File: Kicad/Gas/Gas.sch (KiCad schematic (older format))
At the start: 9 parts, among them J1 MG811, J2 Arduino, J3 MQ135

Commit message: Added air quality sensor to Kicad Gas schematic. Added code for CCS811. Note: arduino program is temporarily not compiling.
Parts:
- added J4: CCS811, Socket_Strips:Socket_Strip_Angled_1x07_Pitch2.54mm, symbol CONN_01X07
- J2: symbol Screw_Terminal_1x06 -> Screw_Terminal_1x10
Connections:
- net +3V3: now also J4.2 (P2)
- net +5V: now also J2.9; no longer J2.3
- net GND: now also J4.1 (P1)
- net Vout: now also J2.3; no longer J2.4
- net at J1.3 (P3): now also J2.10; no longer J2.5
- net nWAKE: now reaches J2.6
- net nWAKE: now also J4.5 (P5)
- new net SCL: J2.5, J4.4 (P4)
- new net SDA: J2.4, J4.3 (P3)
- new net nINT: J2.7, J4.6 (P6)
- new net nRST: J2.8, J4.7 (P7)
- no-connect marks 3 -> 2
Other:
- moved on the sheet: C1, C2, D1, J1, J3, R1, R2, R3

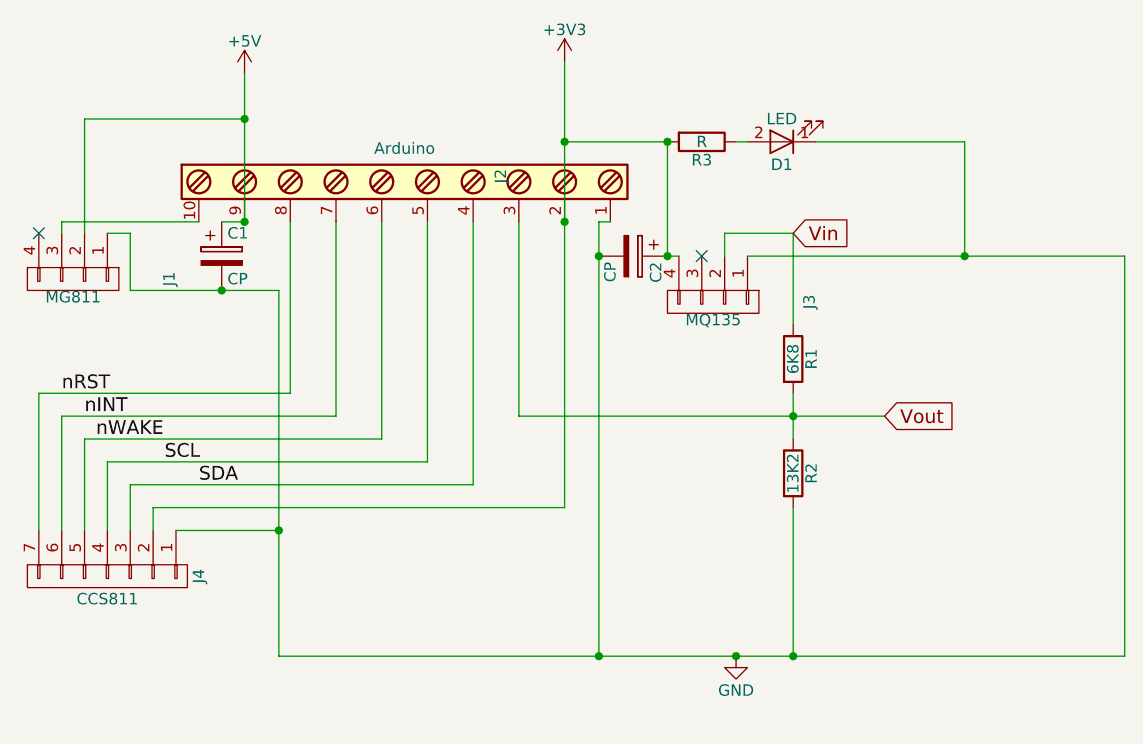
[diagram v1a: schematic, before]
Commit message: Temperature and Temperature+RH (TTRH) sensors are all implemented. All sensors were tested, except Thermopar temperature sensor. Added TTRH shield schematic and layout (missing SDA1 and SCL1 for SHT75).
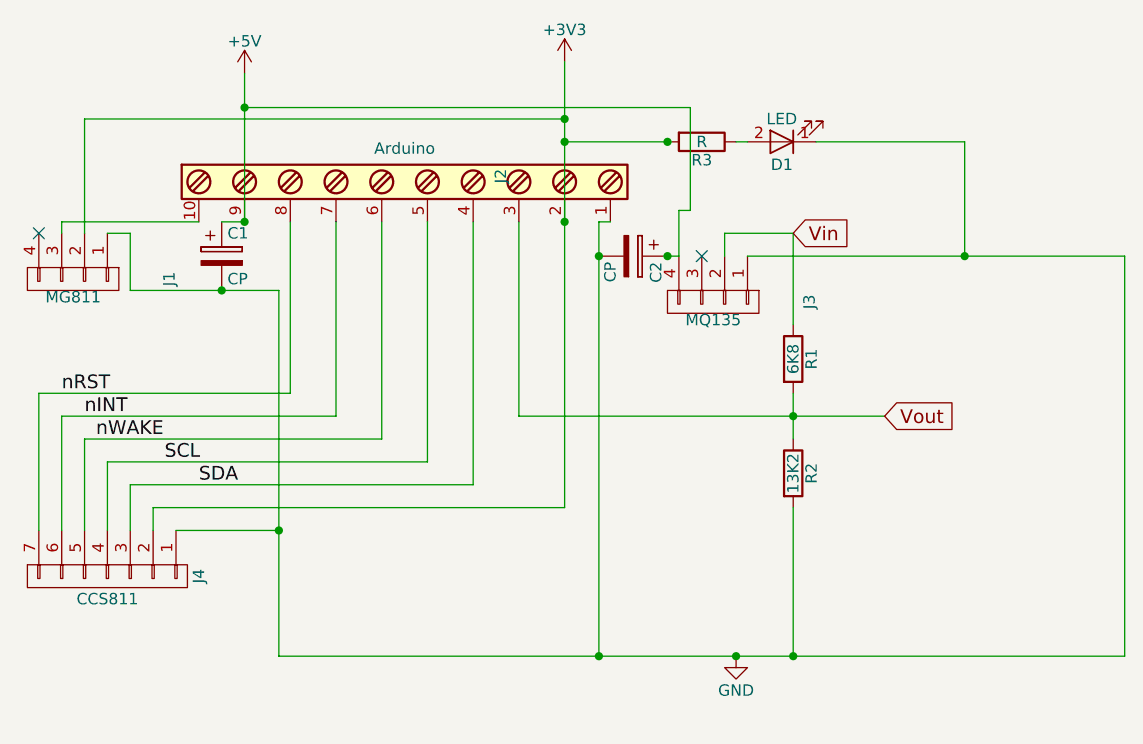
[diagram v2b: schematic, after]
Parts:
- J2: footprint Connectors_Terminal_Blocks:TerminalBlock_Pheonix_MPT-2.54mm_6pol -> Connectors_Terminal_Blocks:TerminalBlock_Pheonix_MPT-2.54mm_10pol
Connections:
- net +3V3: now also J1.2 (P2); no longer C2.1, J3.4 (P4)
- net +5V: now also C2.1, J3.4 (P4); no longer J1.2 (P2)
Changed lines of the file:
@@
 F 0 "J2" H 3050 1700 50  0000 C TNN
 F 1 "Arduino" V 2900 1250 50  0000 C TNN
-F 2 "Connectors_Terminal_Blocks:TerminalBlock_Pheonix_MPT-2.54mm_6pol" H 3050 825 50  0001 C CNN
+F 2 "Connectors_Terminal_Blocks:TerminalBlock_Pheonix_MPT-2.54mm_10pol" H 3050 825 50  0001 C CNN
 F 3 "" H 3025 1450 50  0001 C CNN
 	1    3050 1250
@@
 	4250 1600 4200 1600
 Wire Wire Line
-	4200 1600 4200 1100
-Wire Wire Line
 	4200 1100 3750 1100
 Connection ~ 3750 1100
-Wire Wire Line
-	1650 1000 2350 1000
 Wire Wire Line
 	2350 800  2350 1450
@@
 Wire Wire Line
 	2350 1450 2250 1450
-Connection ~ 2350 1000
 Connection ~ 2350 1450
 Wire Wire Line
@@
 	1450 2200 1450 2800
 Connection ~ 4750 3350
+Wire Wire Line
+	1650 1000 3750 1000
+Connection ~ 3750 1000
+Wire Wire Line
+	4250 1600 4250 1400
+Wire Wire Line
+	4250 1400 4300 1400
+Wire Wire Line
+	4300 1400 4300 950
+Wire Wire Line
+	4300 950  2350 950
+Connection ~ 2350 950
 $EndSCHEMATC

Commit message: Corrected kicad libraries. Added ecoPlanos libs.
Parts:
- removed J2: Arduino, Connectors_Terminal_Blocks:TerminalBlock_Pheonix_MPT-2.54mm_10pol, symbol Screw_Terminal_1x10
- added J2, J5: CONN_01X04, symbol CONN_01X04
- added J6, J7: CONN_01X02, symbol CONN_01X02
- D1: symbol LED -> LED-RESCUE-Gas
- J1: footprint Socket_Strips:Socket_Strip_Angled_1x04_Pitch2.54mm -> Pin_Headers:Pin_Header_Straight_1x03_Pitch1.00mm
- J3: footprint Socket_Strips:Socket_Strip_Angled_1x04_Pitch2.54mm -> Pin_Headers:Pin_Header_Straight_1x04_Pitch2.54mm
- R1, R2, R3: symbol R -> R-RESCUE-Gas
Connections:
- net +3V3: now also C1.1, J6.1 (P1)
- net +5V: now also J7.1 (P1); no longer C1.1
- net GND: now also J6.2 (P2), J7.2 (P2)
- net SCL: now also J5.1 (P1)
- net SDA: now also J5.2 (P2)
- net Vout: now also J5.3 (P3)
- net nINT: now also J2.3 (P3)
- net nRST: now also J2.2 (P2)
- net nWAKE: now also J2.4 (P4)
- net at J1.3 (P3): now also J5.4 (P4)
- net Vin: no longer names the net of J3.2 (P2), R1.1
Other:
- moved on the sheet: C1, C2, D1, J1, R3

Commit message: Added PH4 connectors libs; Finshed CO2 sensors schematic circuit.
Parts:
- J2: value CONN_01X04 -> Digital; footprint (none) -> ecoPlanos_custom:JST_PHR-4; symbol CONN_01X04 -> PHR-4
- J4: footprint Socket_Strips:Socket_Strip_Angled_1x07_Pitch2.54mm -> Pin_Headers:Pin_Header_Straight_1x07_Pitch2.54mm
- J5: value CONN_01X04 -> Analog; footprint (none) -> ecoPlanos_custom:JST_PHR-4; symbol CONN_01X04 -> PHR-4
- J6, J7: footprint (none) -> Socket_Strips:Socket_Strip_Angled_1x02_Pitch2.54mm
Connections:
- no-connect marks 2 -> 4
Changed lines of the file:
@@
 EESchema Schematic File Version 2
+LIBS:ecoPlanos_custom
 LIBS:Gas-rescue
-LIBS:freetronics_schematic
 LIBS:power
 LIBS:device
@@
 LIBS:contrib
 LIBS:valves
-LIBS:mq135
+LIBS:Common-Parts-Library
+LIBS:freetronics_schematic
 LIBS:Gas-cache
 EELAYER 25 0
@@
 $EndDescr
 $Comp
-L GND #PWR2
+L GND #PWR01
 U 1 1 5966646F
 P 4050 3450
-F 0 "#PWR2" H 4050 3200 50  0001 C CNN
+F 0 "#PWR01" H 4050 3200 50  0001 C CNN
 F 1 "GND" H 4050 3300 50  0000 C CNN
 F 2 "" H 4050 3450 50  0001 C CNN
@@
 $EndComp
 $Comp
-L +5V #PWR3
+L +5V #PWR02
 U 1 1 59666483
 P 4250 750
-F 0 "#PWR3" H 4250 600 50  0001 C CNN
+F 0 "#PWR02" H 4250 600 50  0001 C CNN
 F 1 "+5V" H 4250 890 50  0000 C CNN
 F 2 "" H 4250 750 50  0001 C CNN
@@
 $EndComp
 $Comp
-L +3V3 #PWR1
+L +3V3 #PWR03
 U 1 1 59666497
 P 3750 750
-F 0 "#PWR1" H 3750 600 50  0001 C CNN
+F 0 "#PWR03" H 3750 600 50  0001 C CNN
 F 1 "+3V3" H 3750 890 50  0000 C CNN
 F 2 "" H 3750 750 50  0001 C CNN
@@
 U 1 1 596669B3
 P 1600 1850
-F 0 "J1" H 1600 2300 50  0000 C TNN
+F 0 "J1" H 1600 2150 50  0000 C TNN
 F 1 "MG811" V 1650 1850 50  0000 C TNN
 F 2 "Pin_Headers:Pin_Header_Straight_1x03_Pitch1.00mm" H 1600 1425 50  0001 C CNN
@@
 U 1 1 59666EBF
 P 4400 1800
-F 0 "J3" H 4400 2250 50  0000 C TNN
+F 0 "J3" H 4400 2100 50  0000 C TNN
 F 1 "MQ135" V 4450 1800 50  0000 C TNN
 F 2 "Pin_Headers:Pin_Header_Straight_1x04_Pitch2.54mm" H 4400 1375 50  0001 C CNN
@@
 F 0 "J4" H 1750 3400 50  0000 C CNN
 F 1 "CCS811" V 1850 3000 50  0000 C CNN
-F 2 "Socket_Strips:Socket_Strip_Angled_1x07_Pitch2.54mm" H 1750 3000 50  0001 C CNN
+F 2 "Pin_Headers:Pin_Header_Straight_1x07_Pitch2.54mm" H 1750 3000 50  0001 C CNN
 F 3 "" H 1750 3000 50  0001 C CNN
 	1    1750 3000
@@
 nRST
 $Comp
-L CONN_01X04 J5
+L PHR-4 J5
 U 1 1 599D4A0D
-P 3500 1300
-F 0 "J5" H 3500 1550 50  0000 C CNN
-F 1 "CONN_01X04" V 3600 1300 50  0000 C CNN
-F 2 "" H 3500 1300 50  0001 C CNN
-F 3 "" H 3500 1300 50  0001 C CNN
-	1    3500 1300
+P 3450 1800
+F 0 "J5" H 3450 2100 50  0000 C CNN
+F 1 "Analog" V 3650 1800 50  0000 C CNN
+F 2 "ecoPlanos_custom:JST_PHR-4" H 3450 1800 50  0001 C CNN
+F 3 "" H 3450 1800 50  0001 C CNN
+	1    3450 1800
 	0    -1   -1   0
 $EndComp
 $Comp
-L CONN_01X04 J2
+L PHR-4 J2
 U 1 1 599D501A
-P 3000 1300
-F 0 "J2" H 3000 1550 50  0000 C CNN
-F 1 "CONN_01X04" V 3100 1300 50  0000 C CNN
-F 2 "" H 3000 1300 50  0001 C CNN
-F 3 "" H 3000 1300 50  0001 C CNN
-	1    3000 1300
+P 2850 1800
+F 0 "J2" H 2850 2100 50  0000 C CNN
+F 1 "Digital" V 3050 1800 50  0000 C CNN
+F 2 "ecoPlanos_custom:JST_PHR-4" H 2850 1800 50  0001 C CNN
+F 3 "" H 2850 1800 50  0001 C CNN
+	1    2850 1800
 	0    -1   -1   0
 $EndComp
@@
 Connection ~ 4750 2300
 Wire Wire Line
-	1750 2500 3350 2500
+	1750 2500 3300 2500
 Wire Wire Line
 	4750 1500 4750 1900
@@
 	2350 1650 2350 3350
 Wire Wire Line
-	3550 2300 5150 2300
+	3500 2300 5150 2300
 Wire Wire Line
 	5750 1600 4550 1600
@@
 	1850 2800 1850 2600
 Wire Wire Line
-	1850 2600 3450 2600
+	1850 2600 3400 2600
 Wire Wire Line
 	1750 2800 1750 2500
@@
 	1650 2800 1650 2400
 Wire Wire Line
-	1650 2400 3150 2400
+	1650 2400 3000 2400
 Connection ~ 2350 2800
 Wire Wire Line
-	1550 2300 3050 2300
+	1550 2300 2900 2300
 Wire Wire Line
 	1550 2300 1550 2800
 Wire Wire Line
-	1450 2200 2950 2200
+	1450 2200 2800 2200
 Wire Wire Line
 	1450 2200 1450 2800
@@
 	4250 750  4250 1600
 Wire Wire Line
-	3550 2300 3550 1500
-Wire Wire Line
-	3450 2600 3450 1500
-Wire Wire Line
-	3350 2500 3350 1500
-Wire Wire Line
-	3150 2400 3150 1500
-Wire Wire Line
-	3050 2300 3050 1500
-Wire Wire Line
-	2950 2200 2950 1500
+	3500 2300 3500 2100
+Wire Wire Line
+	3400 2600 3400 2100
+Wire Wire Line
+	3300 2500 3300 2100
+Wire Wire Line
+	3000 2400 3000 2100
+Wire Wire Line
+	2900 2300 2900 2100
+Wire Wire Line
+	2800 2200 2800 2100
 Wire Wire Line
 	4050 3200 4050 3450
@@
 Connection ~ 3750 3350
 Wire Wire Line
-	1550 1500 2450 1500
-Wire Wire Line
-	2450 1500 2450 1600
-Wire Wire Line
-	2450 1600 3650 1600
-Wire Wire Line
-	3650 1600 3650 1500
+	1550 1500 3600 1500
+Wire Wire Line
+	3600 1500 3600 2100
 $Comp
 L CONN_01X02 J6
@@
 F 0 "J6" H 6050 1000 50  0000 C CNN
 F 1 "CONN_01X02" V 6150 850 50  0000 C CNN
-F 2 "" H 6050 850 50  0001 C CNN
+F 2 "Socket_Strips:Socket_Strip_Angled_1x02_Pitch2.54mm" H 6050 850 50  0001 C CNN
 F 3 "" H 6050 850 50  0001 C CNN
 	1    6050 850
@@
 F 0 "J7" H 6050 1500 50  0000 C CNN
 F 1 "CONN_01X02" V 6150 1350 50  0000 C CNN
-F 2 "" H 6050 1350 50  0001 C CNN
+F 2 "Socket_Strips:Socket_Strip_Angled_1x02_Pitch2.54mm" H 6050 1350 50  0001 C CNN
 F 3 "" H 6050 1350 50  0001 C CNN
 	1    6050 1350
@@
 	5750 1400 5850 1400
 Connection ~ 5750 1400
+NoConn ~ 2700 2100
+NoConn ~ 3000 1950
 $EndSCHEMATC
